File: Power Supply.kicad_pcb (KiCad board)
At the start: 2 copper layers, 254 x 187.3 mm, 16 parts

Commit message: Schematic should be finished at this point.  Added more commentary to the README, and ensured all components have footprints assigned.
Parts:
- removed REF** (x8): MountingHole_5.5mm_Pad_Via, MountingHole:MountingHole_5.5mm_Pad_Via
- added C4: 18000u 25V, Capacitor_THT:CP_Radial_D35.0mm_P10.00mm_SnapIn, F.Cu at (251.4, 145.5)
- added C8a1: 100u 100V, Capacitor_THT:CP_Radial_D10.0mm_P5.00mm, F.Cu at (145.4, 130.8)
- added C8b1: 100u 100V, Capacitor_THT:CP_Radial_D10.0mm_P5.00mm, F.Cu at (124.2, 130.8)
- added CN1: 26-60-4120, Connector_Molex:Molex_KK-396_A-41791-0012_1x12_P3.96mm_Vertical, F.Cu at (227.2, 206.2)
- added CN10: 26-60-4030, Connector_Molex:Molex_KK-396_A-41791-0003_1x03_P3.96mm_Vertical, F.Cu at (101.1, 74.9)
- added CN2: 26-60-4060, Connector_Molex:Molex_KK-396_A-41791-0006_1x06_P3.96mm_Vertical, F.Cu at (203.5, 221.4)
- added CN3: 26-60-4100, Connector_Molex:Molex_KK-396_A-41791-0010_1x10_P3.96mm_Vertical, F.Cu at (172.9, 221.4)
- added CN4: 26-60-4120, Connector_Molex:Molex_KK-396_A-41791-0012_1x12_P3.96mm_Vertical, F.Cu at (106.6, 217.3)
- added CN5: 26-60-4080, Connector_Molex:Molex_KK-396_A-41791-0008_1x08_P3.96mm_Vertical, F.Cu at (105.7, 50.0)
- added CN6: 26-60-4150, Connector_Molex:Molex_KK-396_A-41791-0015_1x15_P3.96mm_Vertical, F.Cu at (143.9, 50.0)
- added CN7: 26-60-4050, Connector_Molex:Molex_KK-396_A-41791-0005_1x05_P3.96mm_Vertical, F.Cu at (255.9, 221.5)
- added CN8: 26-60-4090, Connector_Molex:Molex_KK-396_A-41791-0009_1x09_P3.96mm_Vertical, F.Cu at (296.3, 221.5)
- added CN9: 26-60-4040, Connector_Molex:Molex_KK-396_A-41791-0004_1x04_P3.96mm_Vertical, F.Cu at (316.9, 221.5)
- added DB1: GBPC1510, Mounts:GBPC_QC, F.Cu at (205.2, 184.7)
- added F1: 7A SB, Mounts:Combo_Blade_Barrel_Fuse, F.Cu at (246.4, 184.5)
- added F2: 7A SB, Mounts:Combo_Blade_Barrel_Fuse, F.Cu at (246.4, 196.5)
- added F4: 8A SB, Mounts:Combo_Blade_Barrel_Fuse, F.Cu at (148.0, 190.0)
- added F5: 4A SB, Mounts:Combo_Blade_Barrel_Fuse, F.Cu at (135.5, 190.0)
- added F6: 5A SB, Mounts:Combo_Blade_Barrel_Fuse, F.Cu at (123.0, 190.0)
- added F7: 1/2A SB 250V, Mounts:Combo_Blade_Barrel_Fuse, F.Cu at (160.5, 190.0)
- H1, H3: footprint MountingHole:MountingHole_5.5mm_Pad_Via -> Mounts:MountingHole_5.5mm_Keyhole
- moved H3 382.8 mm to (334.3, 221.9), turned to -90 degrees
- moved H2 361.4 mm to (334.3, 168.8), turned to -90 degrees
- moved H1 331.4 mm to (334.3, 49.2), turned to -90 degrees
- moved H5 283.7 mm to (214.6, 221.9), turned to -90 degrees
- moved H8 210.0 mm to (94.9, 221.9), turned to -90 degrees
- moved H4 198.7 mm to (214.6, 49.2), turned to -90 degrees
- moved H7 171.0 mm to (94.9, 168.8), turned to -90 degrees
- moved H6 71.1 mm to (94.9, 49.2), turned to -90 degrees
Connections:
- H1 pad 1: (no net) -> unconnected-(H1-Pad1)
- H2 pad 1: (no net) -> unconnected-(H2-Pad1)
- H3 pad 1: (no net) -> unconnected-(H3-Pad1)
- H4 pad 1: (no net) -> unconnected-(H4-Pad1)
- H5 pad 1: (no net) -> unconnected-(H5-Pad1)
- H6 pad 1: (no net) -> unconnected-(H6-Pad1)
- H7 pad 1: (no net) -> unconnected-(H7-Pad1)
- H8 pad 1: (no net) -> unconnected-(H8-Pad1)
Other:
- board text added: "NOTE: Pins 4 and 5 of CN7 may be unused (CN7 plug may be 3-pin instead of 5-pin)"

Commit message: Finished schematic; began placing and routing board. 12V regulation section still not placed, and HV section not routed.
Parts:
- added C1: 2200u 25V, Capacitor_THT:CP_Radial_D12.5mm_P5.00mm, F.Cu at (212.9, 144.6)
- added C10: 150u 200V, Capacitor_THT:CP_Radial_D22.0mm_P10.00mm_SnapIn, F.Cu at (145.5, 132.5)
- added C11: 150u 200V, Capacitor_THT:CP_Radial_D22.0mm_P10.00mm_SnapIn, F.Cu at (173.0, 132.5)
- added C12: 0.1u, Capacitor_THT:C_Rect_L7.0mm_W3.5mm_P5.00mm, F.Cu at (143.0, 76.0)
- added C13: 0.1u, Capacitor_THT:C_Rect_L7.0mm_W3.5mm_P5.00mm, F.Cu at (183.0, 85.5)
- added C14: 22u 25V, Capacitor_THT:CP_Radial_D6.3mm_P2.50mm, F.Cu at (120.0, 61.0)
- added C15: 22u 25V, Capacitor_THT:CP_Radial_D6.3mm_P2.50mm, F.Cu at (120.0, 80.0)
- added C16: 0.1u, Capacitor_THT:C_Rect_L7.0mm_W3.5mm_P5.00mm, F.Cu at (110.5, 71.0)
- added C17: GRM319R61E105KC36D, Capacitor_SMD:C_1206_3216Metric_Pad1.33x1.80mm_HandSolder, F.Cu at (398.0, 205.2)
- added C18: C1206X102J5GACTU, Capacitor_SMD:C_1206_3216Metric_Pad1.33x1.80mm_HandSolder, F.Cu at (398.0, 208.5)
- added C19: C1206C392K5RACTU, Capacitor_SMD:C_1206_3216Metric_Pad1.33x1.80mm_HandSolder, F.Cu at (398.0, 211.8)
- added C2: 0.1u, Capacitor_SMD:C_1206_3216Metric_Pad1.33x1.80mm_HandSolder, F.Cu at (328.2, 103.5)
- added C20: 20TQC100MYF, Capacitor_Tantalum_SMD:CP_EIA-7343-20_Kemet-V_Pad2.25x2.55mm_HandSolder, F.Cu at (389.9, 206.4)
- added C21: 100p, Capacitor_SMD:C_1206_3216Metric_Pad1.33x1.80mm_HandSolder, F.Cu at (303.5, 107.8)
- added C22: 100u 25V, Capacitor_THT:CP_Radial_D6.3mm_P2.50mm, F.Cu at (379.6, 207.4)
- added C23: 100u 25V, Capacitor_THT:CP_Radial_D6.3mm_P2.50mm, F.Cu at (379.6, 215.2)
- added C24: 0.1u, Capacitor_SMD:C_1206_3216Metric_Pad1.33x1.80mm_HandSolder, F.Cu at (278.9, 84.5)
- added C25: 6TPE150M, Capacitor_Tantalum_SMD:CP_EIA-7343-20_Kemet-V_Pad2.25x2.55mm_HandSolder, F.Cu at (322.2, 62.5)
- added C26: EEFCX1E330R, Capacitor_Tantalum_SMD:CP_EIA-7343-20_Kemet-V_Pad2.25x2.55mm_HandSolder, F.Cu at (389.9, 212.2)
- added C3: CGA9N3X7R1H106K230KB, Capacitor_SMD:C_2220_5750Metric_Pad1.97x5.40mm_HandSolder, F.Cu at (335.8, 75.2)
- added C5: DNP, Capacitor_SMD:C_1206_3216Metric_Pad1.33x1.80mm_HandSolder, F.Cu at (302.5, 96.3)
- added C6: 2.2u, Capacitor_SMD:C_1206_3216Metric_Pad1.33x1.80mm_HandSolder, F.Cu at (311.7, 92.5)
- added C7: 0.015u, Capacitor_SMD:C_1206_3216Metric_Pad1.33x1.80mm_HandSolder, F.Cu at (303.5, 111.0)
- added C8: ECPU1C474MA5, Capacitor_SMD:C_1206_3216Metric_Pad1.33x1.80mm_HandSolder, F.Cu at (310.9, 112.7)
- added C9: 0.1u 200V, Capacitor_THT:C_Rect_L4.6mm_W3.0mm_P2.50mm_MKS02_FKP02, F.Cu at (101.2, 136.0)
- added D1: 1N4001, Diode_THT:D_DO-41_SOD81_P10.16mm_Horizontal, F.Cu at (278.0, 183.9)
- added D10: 1N4743, Diode_THT:D_DO-41_SOD81_P12.70mm_Horizontal, F.Cu at (164.7, 90.0)
- added D11: 1N4764, Diode_THT:D_DO-41_SOD81_P12.70mm_Horizontal, F.Cu at (139.2, 86.5)
- added D13: 1N5401, Diode_THT:D_DO-41_SOD81_P10.16mm_Horizontal, F.Cu at (234.0, 215.7)
- added D14: 1N5401, Diode_THT:D_DO-41_SOD81_P10.16mm_Horizontal, F.Cu at (229.5, 215.8)
- added D2: TL431LP, Package_TO_SOT_THT:TO-92_Inline, F.Cu at (292.5, 72.5)
- added D3: 2N6071, Package_TO_SOT_THT:TO-220-3_Vertical, F.Cu at (261.5, 71.5)
- added D4: B330-13-F, Diode_SMD:D_SMC, F.Cu at (390.2, 219.1)
- added D5: 1N4004, Diode_THT:D_DO-41_SOD81_P12.70mm_Horizontal, F.Cu at (177.8, 113.5)
- added D6: 1N5228, Diode_THT:D_DO-41_SOD81_P12.70mm_Horizontal, F.Cu at (164.7, 70.5)
- added D7: 1N4004, Diode_THT:D_DO-41_SOD81_P12.70mm_Horizontal, F.Cu at (177.8, 109.5)
- added D8: 1N5228, Diode_THT:D_DO-41_SOD81_P12.70mm_Horizontal, F.Cu at (165.2, 105.5)
- added D9: 1N4760, Diode_THT:D_DO-41_SOD81_P12.70mm_Horizontal, F.Cu at (177.3, 66.0)
- added F3: 6A, Mounts:BelFuse_0679L, F.Cu at (308.0, 60.0)
- added L1: DR127-4R7-R, Mounts:Eaton_Can_Inductor, F.Cu at (310.6, 79.3)
- added L2: B82477R4302M100, Inductor_SMD:L_TDK_SLF12555, F.Cu at (378.4, 196.5)
- added Q1: IRLZ34N, Package_TO_SOT_THT:TO-220-3_Vertical, F.Cu at (326.6, 74.5)
- added Q2: IRLZ34N, Package_TO_SOT_THT:TO-220-3_Vertical, F.Cu at (326.6, 90.2)
- added Q3: Si7149DP, Package_SO:PowerPAK_SO-8_Single, F.Cu at (390.5, 198.4)
- added R1: 82k, Resistor_SMD:R_1206_3216Metric_Pad1.30x1.75mm_HandSolder, F.Cu at (310.9, 106.2)
- added R10: 330k 1/2W, Resistor_THT:R_Axial_DIN0309_L9.0mm_D3.2mm_P15.24mm_Horizontal, F.Cu at (137.9, 82.0)
- added R11: 330k 1/2W, Resistor_THT:R_Axial_DIN0309_L9.0mm_D3.2mm_P15.24mm_Horizontal, F.Cu at (162.9, 85.5)
- added R12: 1.5k 1/2W, Resistor_THT:R_Axial_DIN0309_L9.0mm_D3.2mm_P15.24mm_Horizontal, F.Cu at (162.9, 75.5)
- added R13: 1.5k, Resistor_THT:R_Axial_DIN0309_L9.0mm_D3.2mm_P15.24mm_Horizontal, F.Cu at (162.9, 95.0)
- added R14: 2k, Resistor_THT:R_Axial_Power_L25.0mm_W9.0mm_P30.48mm, F.Cu at (126.3, 95.5)
- added R15: 130 5W, Resistor_THT:R_Axial_Power_L25.0mm_W9.0mm_P30.48mm, F.Cu at (126.3, 108.5)
- added R16: 1.5k, Resistor_THT:R_Axial_DIN0309_L9.0mm_D3.2mm_P15.24mm_Horizontal, F.Cu at (126.9, 60.5)
- added R17: 1.5k, Resistor_THT:R_Axial_DIN0309_L9.0mm_D3.2mm_P15.24mm_Horizontal, F.Cu at (114.4, 87.5)
- added R18: 1.37k, Resistor_SMD:R_1206_3216Metric_Pad1.30x1.75mm_HandSolder, F.Cu at (373.8, 211.7)
- added R19: 243R, Resistor_SMD:R_1206_3216Metric_Pad1.30x1.75mm_HandSolder, F.Cu at (373.8, 215.0)
- added R2: 487R, Resistor_SMD:R_1206_3216Metric_Pad1.30x1.75mm_HandSolder, F.Cu at (310.9, 109.5)
- added R20: 1.82k, Resistor_SMD:R_1206_3216Metric_Pad1.30x1.75mm_HandSolder, F.Cu at (373.8, 218.3)
- added R21: 300R 1/2W, Resistor_THT:R_Axial_DIN0309_L9.0mm_D3.2mm_P15.24mm_Horizontal, F.Cu at (283.0, 183.9)
- added R22: 3k, Resistor_THT:R_Axial_DIN0309_L9.0mm_D3.2mm_P15.24mm_Horizontal, F.Cu at (271.8, 69.4)
- added R23: 1.8k, Resistor_THT:R_Axial_DIN0309_L9.0mm_D3.2mm_P15.24mm_Horizontal, F.Cu at (271.8, 74.2)
- added R24: 220, Resistor_THT:R_Axial_DIN0309_L9.0mm_D3.2mm_P15.24mm_Horizontal, F.Cu at (271.8, 78.9)
- added R25: 10k, Resistor_SMD:R_1206_3216Metric_Pad1.30x1.75mm_HandSolder, F.Cu at (373.8, 221.6)
- added R3: 73.2k, Resistor_SMD:R_1206_3216Metric_Pad1.30x1.75mm_HandSolder, F.Cu at (303.5, 101.2)
- added R4: 10k, Resistor_SMD:R_1206_3216Metric_Pad1.30x1.75mm_HandSolder, F.Cu at (303.5, 104.5)
- added R5: 105k, Resistor_SMD:R_1206_3216Metric_Pad1.30x1.75mm_HandSolder, F.Cu at (373.8, 205.1)
- added R6: 2.21k, Resistor_SMD:R_1206_3216Metric_Pad1.30x1.75mm_HandSolder, F.Cu at (373.8, 208.4)
- added R7: CRA2512-FZ-R010ELF, Resistor_SMD:R_2512_6332Metric_Pad1.40x3.35mm_HandSolder, F.Cu at (399.1, 197.6)
- added R8: 47k 1W, Resistor_THT:R_Axial_DIN0309_L9.0mm_D3.2mm_P15.24mm_Horizontal, F.Cu at (162.9, 80.5)
- added R9: 47k 1W, Resistor_THT:R_Axial_DIN0309_L9.0mm_D3.2mm_P15.24mm_Horizontal, F.Cu at (162.9, 100.5)
- added REF**: ESD-Logo_13.2x12mm_SilkScreen, Symbol:ESD-Logo_13.2x12mm_SilkScreen, F.Cu at (97.0, 145.2)
- added REF**: Symbol_HighVoltage_Triangle_8x7mm_Copper, Symbol:Symbol_HighVoltage_Triangle_8x7mm_Copper, F.Cu at (196.0, 133.5)
- added RY1: J107F1CS2024VDC.80, Mounts:J107F_Relays, F.Cu at (295.5, 196.5)
- added TP1: TestPoint, TestPoint:TestPoint_Loop_D2.60mm_Drill1.4mm_Beaded, F.Cu at (152.5, 150.0)
- added TR1: MPSA92, Package_TO_SOT_THT:TO-92_Inline, F.Cu at (186.6, 70.7)
- added TR2: MPSA42, Package_TO_SOT_THT:TO-92_Inline, F.Cu at (186.6, 99.2)
- added TR3: MJE15030, Package_TO_SOT_THT:TO-220-3_Vertical, F.Cu at (197.6, 68.0)
- added TR4: MJE15031, Package_TO_SOT_THT:TO-220-3_Vertical, F.Cu at (197.6, 97.5)
- added TR6: MJE15030, Package_TO_SOT_THT:TO-220-3_Vertical, F.Cu at (118.4, 98.0)
- added U1: LM3150MH, Package_SO:HTSSOP-14-1EP_4.4x5mm_P0.65mm_EP3.4x5mm_Mask3x3.1mm, F.Cu at (311.8, 97.5)
- added U2: LM5085MY/NOPB, Package_SO:HVSSOP-8-1EP_3x3mm_P0.65mm_EP1.57x1.89mm_ThermalVias, F.Cu at (399.3, 217.6)
- added U3: LM2991, Package_TO_SOT_THT:TO-220-5_Vertical, F.Cu at (388.4, 193.1)
- added VR1: LM7812_TO220, Package_TO_SOT_THT:TO-220-3_Vertical, F.Cu at (123.6, 69.0)
- added Z1: MOV-14D470K, Varistor:RV_Disc_D21.5mm_W6.1mm_P7.5mm, F.Cu at (98.5, 128.0)
- moved F2 55.0 mm to (207.0, 158.0)
- moved DB1 52.0 mm to (248.7, 156.3)
- moved CN1 46.9 mm to (181.7, 194.5), turned to 0 degrees
- moved F1 41.8 mm to (207.0, 170.5)
- moved C4 31.5 mm to (252.5, 114.0)
- moved C8a1 28.1 mm to (117.6, 135.5)
- moved C8b1 10.6 mm to (117.6, 122.5)
- moved CN7 0.14 mm to (255.9, 221.4)
- moved CN8 0.14 mm to (296.3, 221.4)
- moved CN9 0.14 mm to (316.9, 221.4)
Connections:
- net Net-(CN1-Pin_1) renamed /+18V
- net Net-(CN1-Pin_10) renamed /9VAC_2
- net Net-(CN1-Pin_11) renamed /9VAC_1
- net Net-(CN1-Pin_2) renamed /+32VA
- net Net-(CN1-Pin_3) renamed /+32VB
- net Net-(CN3-Pin_4) renamed /+32VB_F
- net Net-(CN3-Pin_6) renamed /+32VA_F
- net Net-(CN4-Pin_5) renamed /+18V_F
- net Net-(CN5-Pin_6) renamed /+5V_F
- CN4 pad 1: Net-(CN4-Pin_1) -> GND
- CN4 pad 10: Net-(CN4-Pin_10) -> GND
- CN4 pad 11: Net-(CN4-Pin_10) -> GND
- CN4 pad 12: Net-(CN4-Pin_10) -> GND
- CN4 pad 2: Net-(CN4-Pin_1) -> GND
- CN4 pad 3: Net-(CN4-Pin_1) -> GND
- CN4 pad 4: Net-(CN4-Pin_1) -> GND
- CN4 pad 9: Net-(CN4-Pin_10) -> GND
- DB1 pad 3: /+12VU -> Net-(D14-K)
- F1 pad 2: /+12VU -> Net-(D14-K)
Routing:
- net GND: track 0.08 -> 647.8 mm, vias 0 -> 11
- net /+12VU: track 0.00 -> 211.5 mm, vias 0 -> 6
- net /+5V_F: track 0.00 -> 189.6 mm
- net /+32VA_F: track 0.00 -> 176.1 mm, vias 0 -> 2
- net /+18V_F: track 0.00 -> 145.5 mm
- net Net-(D14-K): track 0.00 -> 124.9 mm
- net /+32VB: track 0.00 -> 112.5 mm, vias 0 -> 12
- net /High Voltage Supplies/100VAC: track 0.00 -> 112.3 mm
- net /High Voltage Supplies/90VAC: track 0.00 -> 112.3 mm, vias 0 -> 1
- net Net-(CN8-Pin_1): track 0.00 -> 104.9 mm
- net /12V Supplies/+12V_REG: track 0.00 -> 98.1 mm
- net /+32VA: track 0.00 -> 93.4 mm
- net /High Voltage Supplies/HV_COM: track 0.00 -> 89.0 mm
- net /9VAC_1: track 0.00 -> 88.4 mm
- net Net-(D13-K): track 0.00 -> 87.3 mm
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- added copper zone on F.Cu, net /+12VU
- added copper zone on B.Cu, net /+32VB
- added copper zone on F.Cu, net /+5V_F
- added copper zone on F.Cu, net /5V_Supply/+5V
- added copper zone on B.Cu, net GND
- added copper zone on F.Cu, net GND
- added copper zone on F.Cu, net Net-(Q1-S)
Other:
- board text added: "*"
- board text added: "+"
- board text added: "+12VU"
- board text added: "+18V LAMPS"
- board text added: "+32V SOLENOIDS"
- board text added: "+5V CROWBAR"
- board text added: "+5V SUPPLY"
- board text added: "-12VU"
- board text added: "9V~"
- board text added: "GROUND REF"
- board text added: "HIGH VOLTAGE"
- board text added: "NOTE: CN3 Pin 10 may be absent"
- board text added: "NOTE: CN7 Pins 4 and 5 may be absent"
- board text added: "▼"
- board text removed: "NOTE: Pins 4 and 5 of CN7 may be unused (CN7 plug may be 3-pin instead of 5-pin)"

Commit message: Finished routing. While DRC fails with some errors, some can be disregarded. Need to do some cleanups to get rid of the others.
Also, added 3 discharge resistors to the schematic.
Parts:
- added R26: 5.1k, Resistor_THT:R_Axial_DIN0309_L9.0mm_D3.2mm_P15.24mm_Horizontal, F.Cu at (196.6, 144.5)
- added R27: 5.1k, Resistor_THT:R_Axial_DIN0309_L9.0mm_D3.2mm_P15.24mm_Horizontal, F.Cu at (285.5, 108.2)
- added R28: 100k, Resistor_THT:R_Axial_DIN0309_L9.0mm_D3.2mm_P15.24mm_Horizontal, F.Cu at (112.4, 118.0)
- moved C23 215.4 mm to (208.8, 84.0)
- moved U3 202.3 mm to (213.5, 91.5), turned to -90 degrees
- moved R19 195.6 mm to (210.2, 107.8), turned to 180 degrees
- moved R20 194.9 mm to (210.2, 112.2)
- moved C22 186.4 mm to (214.0, 121.8)
- moved C20 114.2 mm to (282.2, 168.2), turned to -90 degrees
- moved C19 103.8 mm to (298.5, 182.2)
- moved C18 103.6 mm to (298.5, 179.5)
- moved C17 100.1 mm to (298.6, 193.5)
- moved C26 98.6 mm to (318.0, 144.8)
- moved U2 97.6 mm to (308.4, 182.0)
- moved R7 97.0 mm to (311.0, 156.9), turned to -90 degrees
- moved L2 88.4 mm to (297.2, 161.8), turned to 180 degrees
- moved Q3 86.7 mm to (310.2, 165.6), turned to -90 degrees
- moved D4 84.4 mm to (318.5, 174.7), turned to -90 degrees
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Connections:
- net Net-(CN5-Pin_5) renamed /+12V_DISP
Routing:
- net GND: track 647.8 -> 906.7 mm, vias 11 -> 32
- net /12V Supplies/+12V_REG: track 98.1 -> 269.0 mm, vias 0 -> 12
- net /+12VU: track 211.5 -> 377.3 mm
- net /+18V_F: track 145.5 -> 303.1 mm, vias 0 -> 2
- net /High Voltage Supplies/-110VDC: track 0.00 -> 143.8 mm
- net /12V Supplies/-12V_REG: track 0.00 -> 141.7 mm
- net Net-(CN8-Pin_6): track 15.3 -> 141.7 mm
- net /High Voltage Supplies/+68VDC: track 0.00 -> 103.0 mm
- net Net-(D6-K): track 0.00 -> 81.1 mm, vias 0 -> 1
- net /-12VU: track 26.3 -> 106.6 mm
- net Net-(D10-K): track 0.00 -> 54.4 mm
- net /High Voltage Supplies/-98VDC: track 0.00 -> 52.1 mm
- net /+5V_F: track 189.6 -> 238.5 mm
- net Net-(U2-ISEN): track 0.00 -> 47.3 mm, vias 0 -> 2
- net Net-(Q3-G): track 0.00 -> 41.3 mm, vias 0 -> 2
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- added copper zone on B.Cu, net /12V Supplies/+12V_REG
- added copper zone on F.Cu, net /12V Supplies/+12V_REG
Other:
- board text added: "+12V SUPPLY"
- board text added: "-12V SUPPLY"

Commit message: First generation of gerber files; will plot to a PDF so it can be printed to scale and dimensions/hole locations verified.
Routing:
- net /+5V_F: track 238.5 -> 237.8 mm
- net GND: vias 32 -> 31

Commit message: Final version, though yet untested.
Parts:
- removed C8: ECPU1C474MA5, Capacitor_SMD:C_1206_3216Metric_Pad1.33x1.80mm_HandSolder
- added C27: 0.47u, Capacitor_SMD:C_1206_3216Metric_Pad1.33x1.80mm_HandSolder, F.Cu at (310.9, 112.6)
- C9: footprint Capacitor_THT:C_Rect_L4.6mm_W3.0mm_P2.50mm_MKS02_FKP02 -> Capacitor_THT:C_Rect_L7.0mm_W3.5mm_P2.50mm_P5.00mm
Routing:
- net GND: track 906.7 -> 909.8 mm
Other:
- board text added: "Layout (C) 2025 E. Reischer LV supply design (C) 2025 E. Reischer HV Supply design (C) Data East Pinball"
- board text added: "Power supply for Data East DMD machines Replacement for 520-5047-00 520-5047-01 520-5047-02"

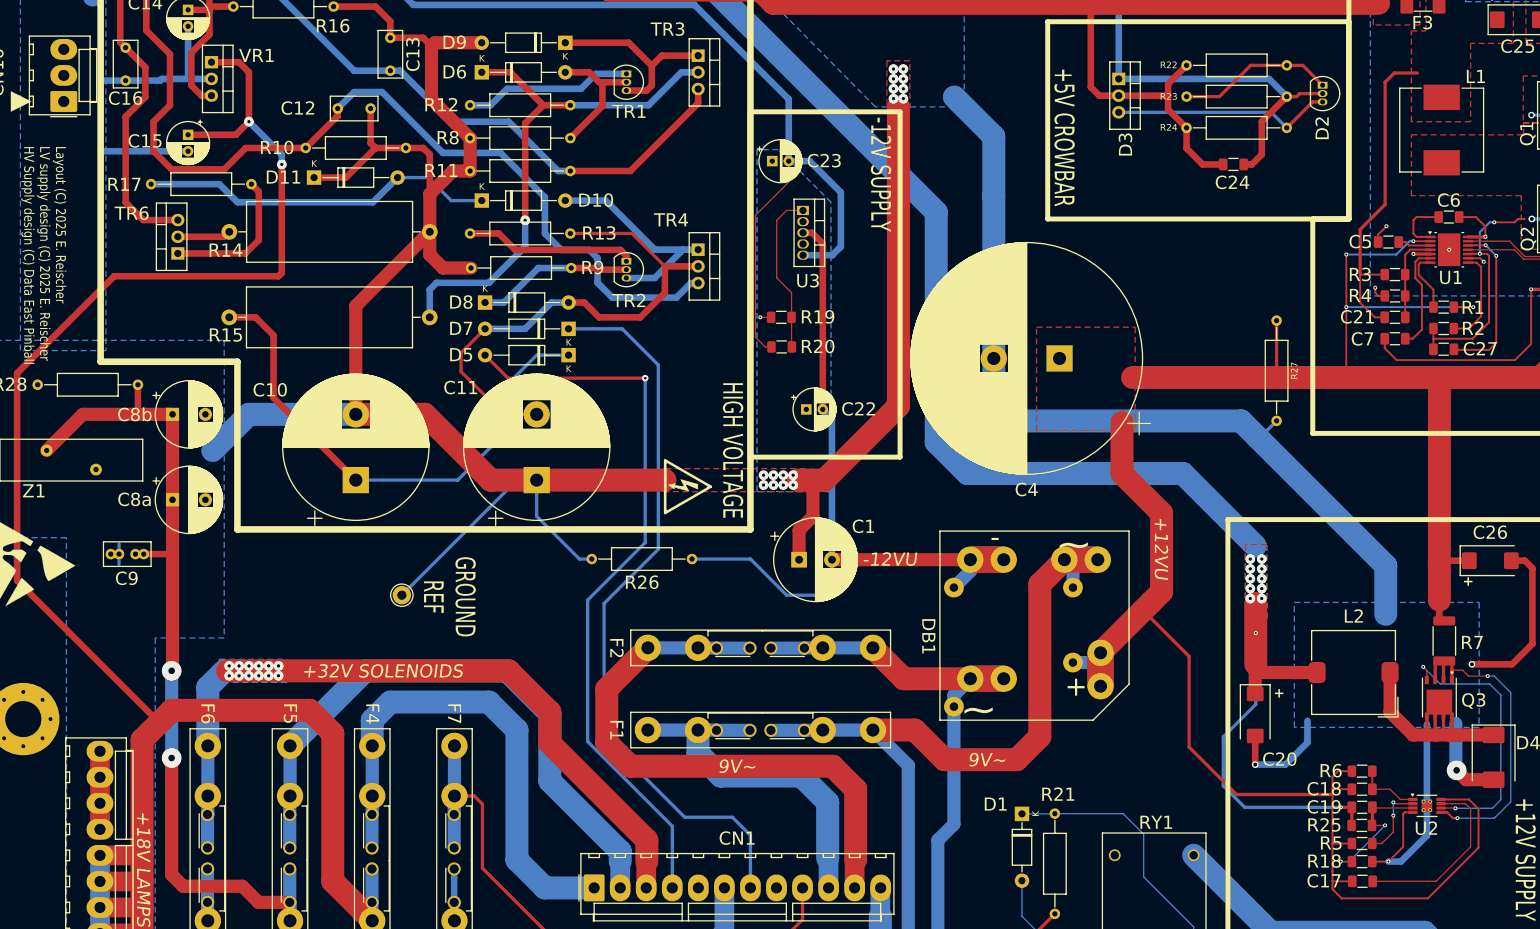
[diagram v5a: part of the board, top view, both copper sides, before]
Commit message: Changed TO-92 packages to non-inlined versions for easier soldering Fixed issue with HV section input voltage; the original schematics are wrong in that the power should come exclusively from the 100V (or 90V) AC supply, and not one from each for positive/negative. Increased the drill sizes of some packages to better fit larger wires from devices in BOM. Assigned an unused pin on CN1 to use as a key, so it cannot be cross-plugged with CN4.
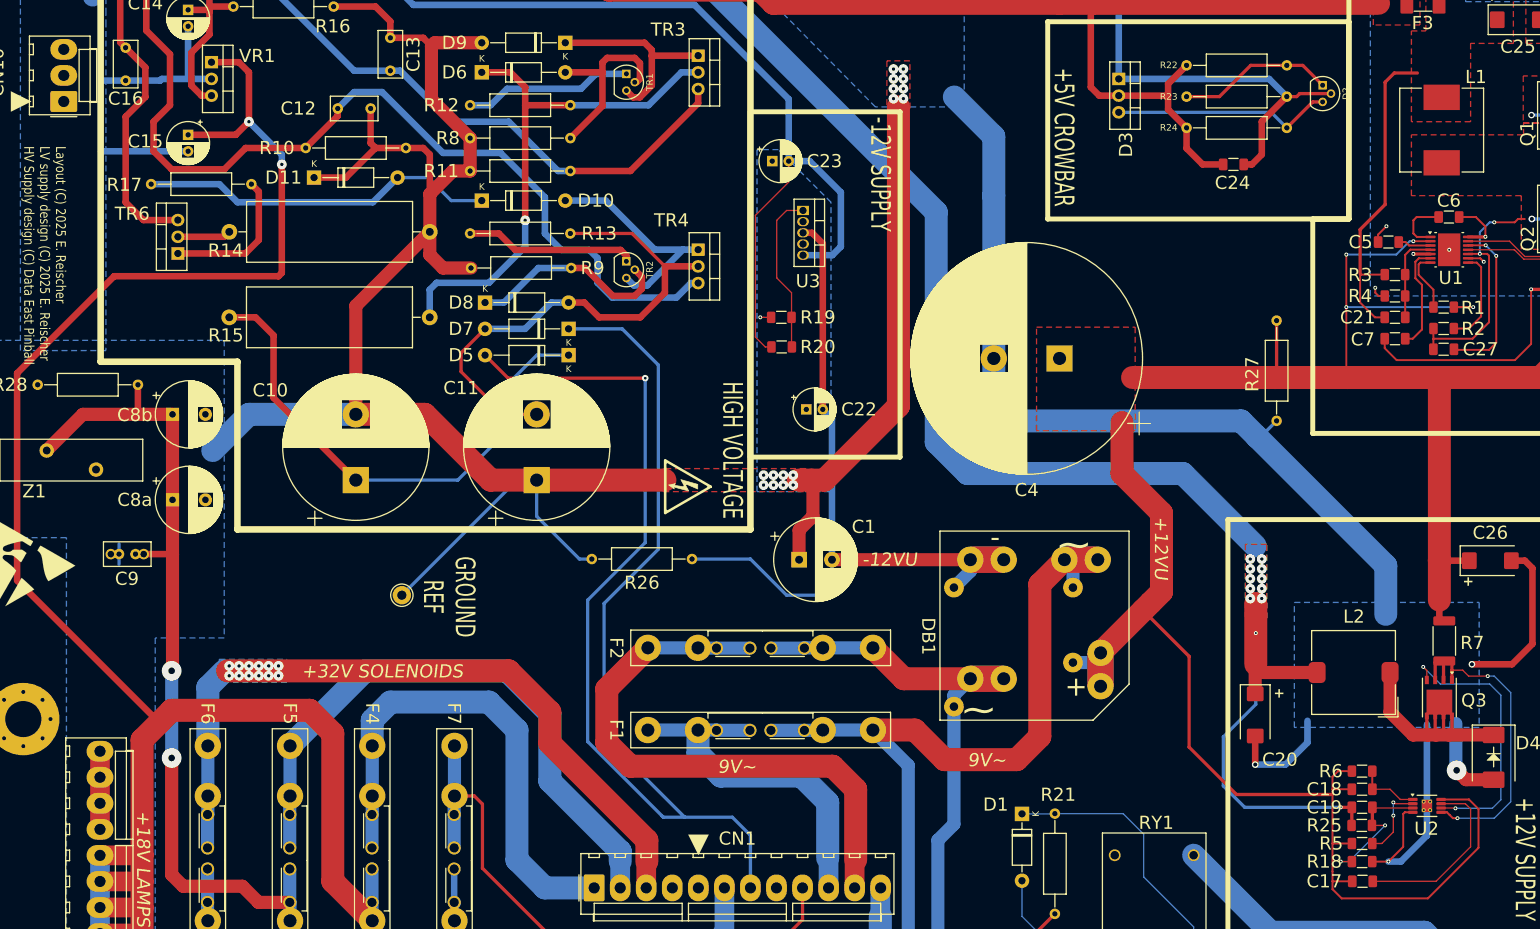
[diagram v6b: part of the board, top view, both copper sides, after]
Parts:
- D2, TR1, TR2: footprint Package_TO_SOT_THT:TO-92_Inline -> Package_TO_SOT_THT:TO-92
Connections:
- D5 pad 2: /High Voltage Supplies/90VAC -> /High Voltage Supplies/100VAC
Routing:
- net /High Voltage Supplies/90VAC: track 112.3 -> 0.00 mm, vias 1 -> 0
- net /High Voltage Supplies/100VAC: track 112.3 -> 216.5 mm, vias 0 -> 1
- net Net-(D6-A): track 20.4 -> 28.9 mm
- net Net-(D8-K): track 23.8 -> 31.6 mm
- net Net-(D9-K): track 29.5 -> 31.1 mm
- net GND: track 909.8 -> 911.1 mm
- net Net-(D10-A): track 33.7 -> 34.7 mm
